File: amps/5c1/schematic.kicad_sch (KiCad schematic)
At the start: 21 parts, among them T1 SE 5k:8

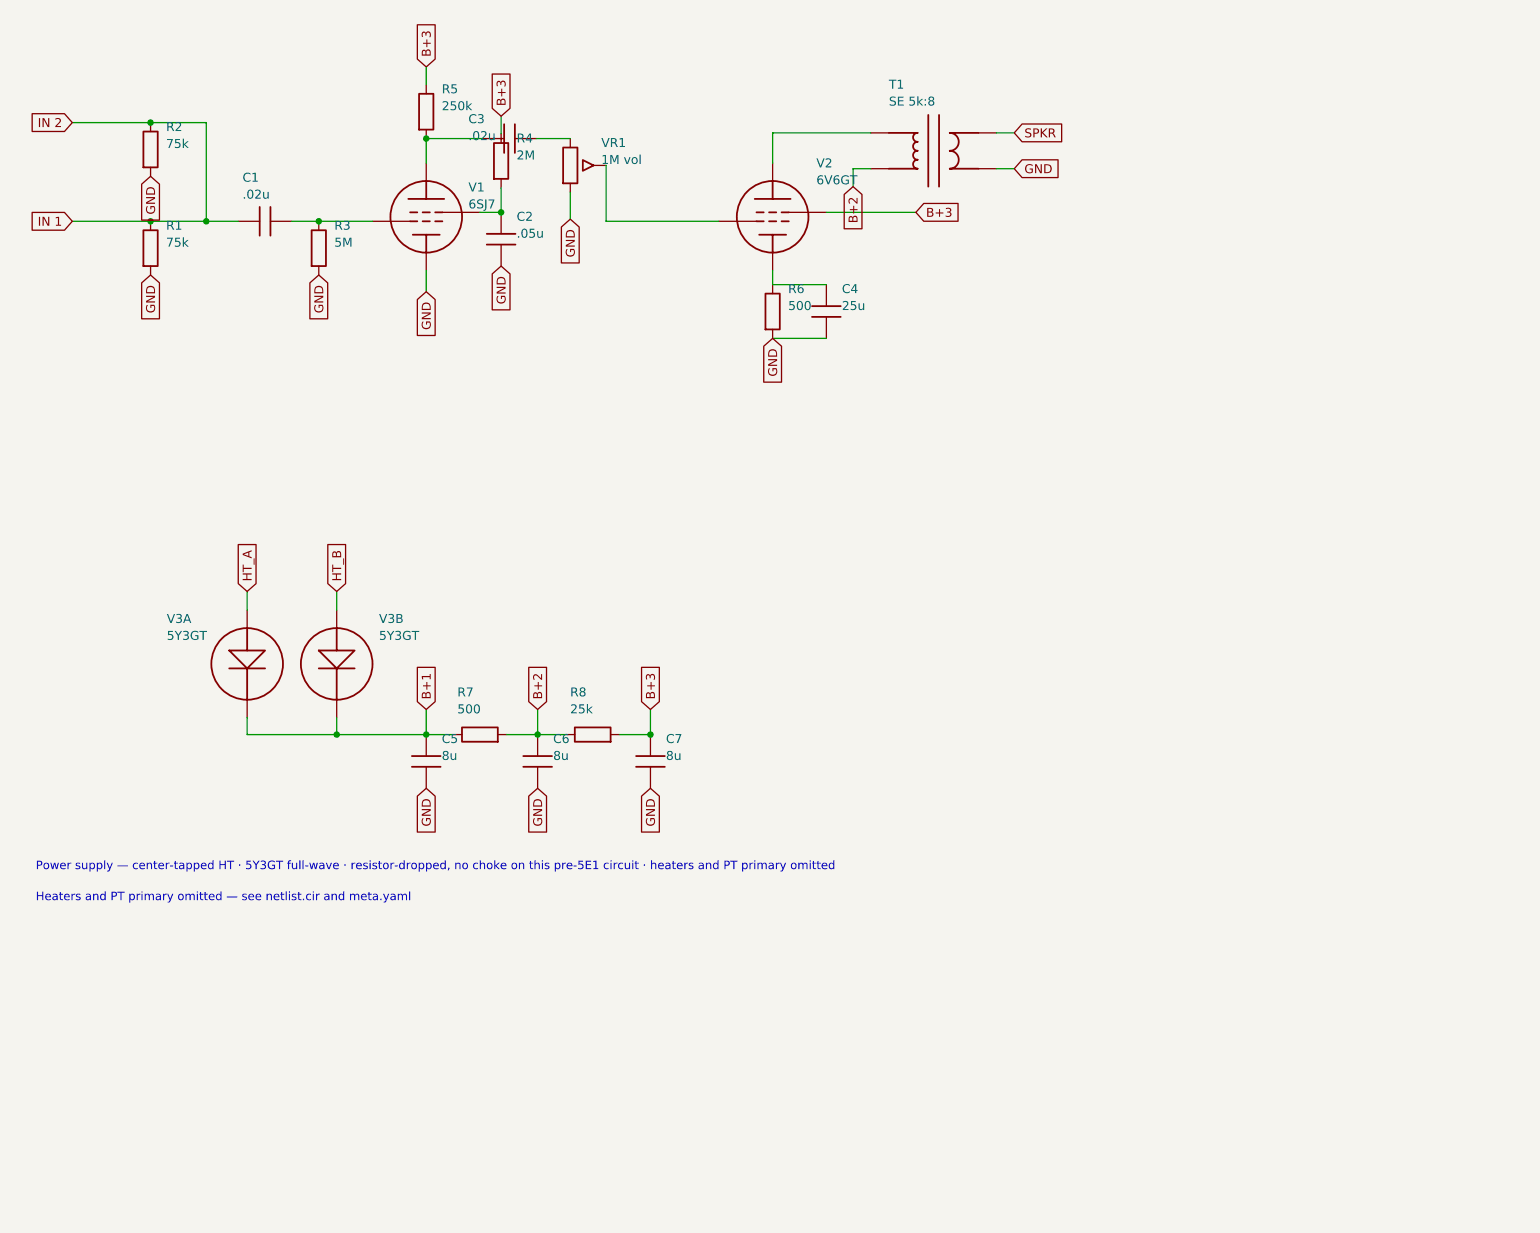
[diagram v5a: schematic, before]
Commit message: Add: real tube pin numbers and readable valve glyphs on every schematic
Phase B of the drawing program. A factory service sheet numbers every tube
pin, because the number is what a technician puts a probe on. This corpus
printed none, and the numbers hidden in its symbols were positional
placeholders (P=1, G=2, K=3) that would have published a 6V6GT's plate as
pin 1 when it is pin 3.

1055 electrodes now carry the real number, 1027 lettered (27 are shared
filaments deduped, 1 dropped for want of clear space on the 6G2). Resolved per
instance from reference/tubes/<slug>.yaml through the same alias resolution the
layout renderer uses, so a 12AX7 section and a 6SL7 section each get their own
basing. A valve whose basing the corpus does not carry prints nothing rather
than a wrong number.

Section letters and basing units are now separate things, which cost a detour
worth recording. The RCA 12AX7-A sheet reads "Pin 1 - Plate of Unit No.2 ...
Pin 6 - Plate of Unit No.1", so unit numbering is not pin order; the 5Y3 and
GZ34 number their units in opposite pin order, so nothing positional can
express it. But the section LETTER is a designator, not a basing fact: this
corpus, like every technician, calls the first stage in signal order V1A, and
five amps' prose already did. On four amps the factory sheets put that first
stage on the other half -- the AA764's own schematic prints +200 V on pin 1 --
so those drawings now state their unit explicitly, each citing its source, and
no letter, netlist, parts list or layout comment changed. 183 layout comments
agree with the printed numbers, 0 disagree. A guard fires if two halves of one
bottle resolve to the same unit, which is exactly how this was found.

Glyphs: the cathode gains a bracket and filament hairpin so it can no longer be
confused with the plate bar, the pentode's screen sits on its own row, and a
rectifier draws as one envelope over its sections instead of two apparent
bottles. Line weights are scaled per sheet to a co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
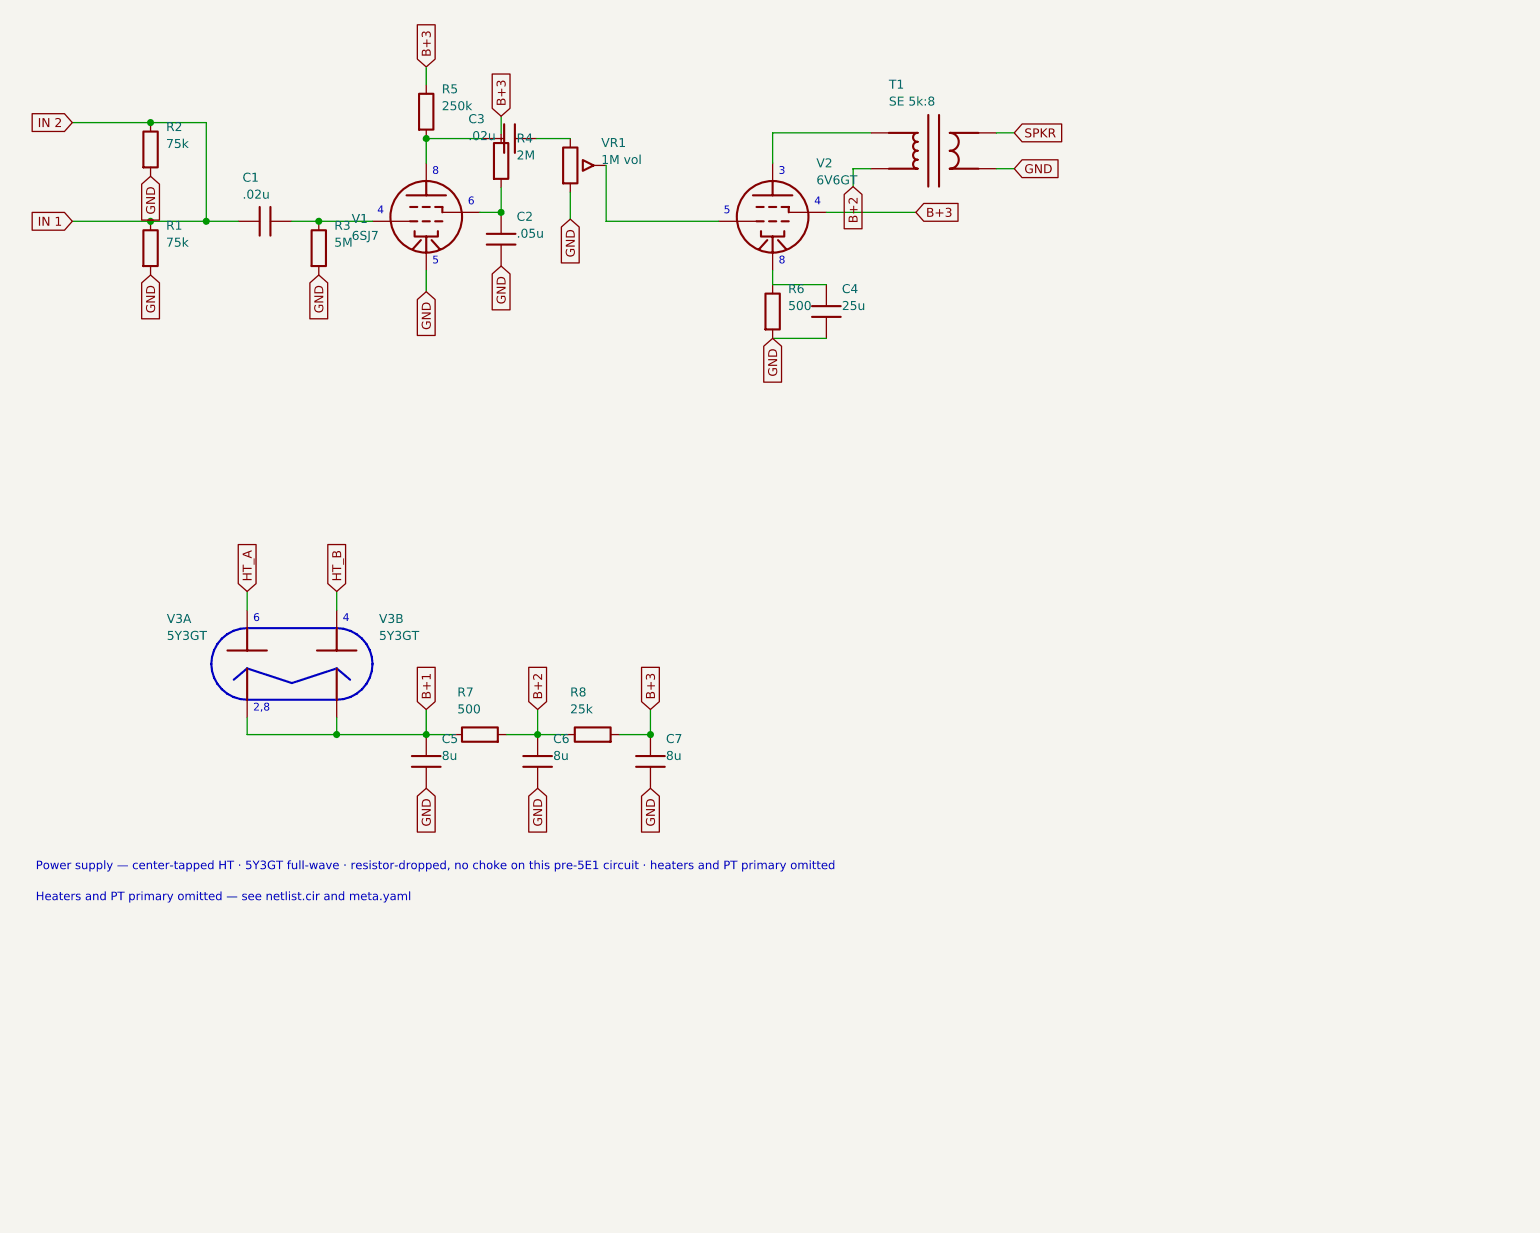
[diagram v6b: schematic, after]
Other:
- note added: "2,8"
- note added: "3"
- note added: "4"
- note added: "5"
- note added: "6"
- note added: "8"
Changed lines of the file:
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@@
   (wire (pts (xy 17.8816 38.913) (xy 28.9816 38.913))
     (stroke (width 0) (type default)))
-  (junction (at 28.9816 38.913) (diameter 0) (color 0 0 0 0))
+  (junction (at 28.9816 38.913) (diameter 1) (color 0 0 0 0))
   (symbol (lib_id "cx:R") (at 28.9816 42.723 0) (unit 1)
     (in_bom yes) (on_board yes)
@@
   (wire (pts (xy 17.8816 24.913) (xy 28.9816 24.913))
     (stroke (width 0) (type default)))
-  (junction (at 28.9816 24.913) (diameter 0) (color 0 0 0 0))
+  (junction (at 28.9816 24.913) (diameter 1) (color 0 0 0 0))
   (symbol (lib_id "cx:R") (at 28.9816 28.723 0) (unit 1)
     (in_bom yes) (on_board yes)
@@
   (wire (pts (xy 36.8816 24.913) (xy 36.8816 38.913))
     (stroke (width 0) (type default)))
-  (junction (at 36.8816 38.913) (diameter 0) (color 0 0 0 0))
+  (junction (at 36.8816 38.913) (diameter 1) (color 0 0 0 0))
   (symbol (lib_id "cx:C") (at 45.2216 38.913 90) (unit 1)
     (in_bom yes) (on_board yes)
@@
   (wire (pts (xy 49.0316 38.913) (xy 52.8416 38.913))
     (stroke (width 0) (type default)))
-  (junction (at 52.8416 38.913) (diameter 0) (color 0 0 0 0))
+  (junction (at 52.8416 38.913) (diameter 1) (color 0 0 0 0))
   (symbol (lib_id "cx:R") (at 52.8416 42.723 0) (unit 1)
     (in_bom yes) (on_board yes)
@@
   (symbol (lib_id "cx:PENTODE") (at 68.0816 38.278 0) (unit 1)
     (in_bom yes) (on_board yes)
-    (property "Reference" "V1" (at 74.0616 34.098 0) (effects (font (size 1.27 1.27)) (justify left)))
-    (property "Value" "6SJ7" (at 74.0616 36.498 0) (effects (font (size 1.27 1.27)) (justify left))))
+    (property "Reference" "V1" (at 57.5067 38.558 0) (effects (font (size 1.27 1.27)) (justify left)))
+    (property "Value" "6SJ7" (at 57.5067 40.958 0) (effects (font (size 1.27 1.27)) (justify left))))
   (wire (pts (xy 68.0816 45.898) (xy 68.0816 48.898))
     (stroke (width 0) (type default)))
@@
   (global_label "B+3" (shape input) (at 68.0816 17.018 90)
     (effects (font (size 1.27 1.27)) (justify left)))
-  (junction (at 68.0816 27.178) (diameter 0) (color 0 0 0 0))
+  (junction (at 68.0816 27.178) (diameter 1) (color 0 0 0 0))
   (wire (pts (xy 68.0816 27.178) (xy 76.0816 27.178))
     (stroke (width 0) (type default)))
@@
   (wire (pts (xy 75.7016 37.643) (xy 78.7016 37.643))
     (stroke (width 0) (type default)))
-  (junction (at 78.7016 37.643) (diameter 0) (color 0 0 0 0))
+  (junction (at 78.7016 37.643) (diameter 1) (color 0 0 0 0))
   (symbol (lib_id "cx:C") (at 78.7016 41.453 0) (unit 1)
     (in_bom yes) (on_board yes)
@@
   (wire (pts (xy 55.3816 111.713) (xy 68.0816 111.713))
     (stroke (width 0) (type default)))
-  (junction (at 55.3816 111.713) (diameter 0) (color 0 0 0 0))
-  (junction (at 68.0816 111.713) (diameter 0) (color 0 0 0 0))
+  (junction (at 55.3816 111.713) (diameter 1) (color 0 0 0 0))
+  (junction (at 68.0816 111.713) (diameter 1) (color 0 0 0 0))
   (symbol (lib_id "cx:C") (at 68.0816 115.523 0) (unit 1)
     (in_bom yes) (on_board yes)
@@
   (wire (pts (xy 79.5016 111.713) (xy 83.8816 111.713))
     (stroke (width 0) (type default)))
-  (junction (at 83.8816 111.713) (diameter 0) (color 0 0 0 0))
+  (junction (at 83.8816 111.713) (diameter 1) (color 0 0 0 0))
   (symbol (lib_id "cx:C") (at 83.8816 115.523 0) (unit 1)
     (in_bom yes) (on_board yes)
@@
   (wire (pts (xy 95.5016 111.713) (xy 99.8816 111.713))
     (stroke (width 0) (type default)))
-  (junction (at 99.8816 111.713) (diameter 0) (color 0 0 0 0))
+  (junction (at 99.8816 111.713) (diameter 1) (color 0 0 0 0))
   (symbol (lib_id "cx:C") (at 99.8816 115.523 0) (unit 1)
     (in_bom yes) (on_board yes)
@@
   (global_label "B+3" (shape input) (at 99.8816 108.153 90)
     (effects (font (size 1.27 1.27)) (justify left)))
+  (polyline (pts (xy 55.3816 96.613) (xy 56.3726 96.711) (xy 57.3256 97) (xy 58.2036 97.469) (xy 58.9736 98.101) (xy 59.6056 98.871) (xy 60.0746 99.749) (xy 60.3636 100.702) (xy 60.4616 101.693) (xy 60.3636 102.684) (xy 60.0746 103.637) (xy 59.6056 104.515) (xy 58.9736 105.285) (xy 58.2036 105.917) (xy 57.3256 106.386) (xy 56.3726 106.675) (xy 55.3816 106.773) (xy 42.6816 106.773) (xy 41.6906 106.675) (xy 40.7376 106.386) (xy 39.8596 105.917) (xy 39.0896 105.285) (xy 38.4576 104.515) (xy 37.9886 103.637) (xy 37.6996 102.684) (xy 37.6016 101.693) (xy 37.6996 100.702) (xy 37.9886 99.749) (xy 38.4576 98.871) (xy 39.0896 98.101) (xy 39.8596 97.469) (xy 40.7376 97) (xy 41.6906 96.711) (xy 42.6816 96.613) (xy 55.3816 96.613))
+    (stroke (width 0.3) (type default) (color 197 163 255 1)) (fill (type none)))
+  (polyline (pts (xy 40.7816 103.928) (xy 42.6816 102.328) (xy 49.0316 104.408) (xy 55.3816 102.328) (xy 57.2816 103.928))
+    (stroke (width 0.3) (type default) (color 197 163 255 1)) (fill (type none)))
+  (text "8" (at 68.9316 31.928 0)
+    (effects (font (size 1.1 1.1)) (justify left)))
+  (text "4" (at 61.1344 37.513 0)
+    (effects (font (size 1.1 1.1)) (justify left)))
+  (text "6" (at 73.9816 36.243 0)
+    (effects (font (size 1.1 1.1)) (justify left)))
+  (text "5" (at 68.9316 44.628 0)
+    (effects (font (size 1.1 1.1)) (justify left)))
+  (text "3" (at 118.062 31.928 0)
+    (effects (font (size 1.1 1.1)) (justify left)))
+  (text "5" (at 110.264 37.513 0)
+    (effects (font (size 1.1 1.1)) (justify left)))
+  (text "4" (at 123.112 36.243 0)
+    (effects (font (size 1.1 1.1)) (justify left)))
+  (text "8" (at 118.062 44.628 0)
+    (effects (font (size 1.1 1.1)) (justify left)))
+  (text "6" (at 43.5316 95.343 0)
+    (effects (font (size 1.1 1.1)) (justify left)))
+  (text "2,8" (at 43.5316 108.043 0)
+    (effects (font (size 1.1 1.1)) (justify left)))
+  (text "4" (at 56.2316 95.343 0)
+    (effects (font (size 1.1 1.1)) (justify left)))
   (text "Power supply — center-tapped HT · 5Y3GT full-wave · resistor-dropped, no choke on this pre-5E1 circuit · heaters and PT primary omitted" (at 12.7 130.491 0)
     (effects (font (size 1.2 1.2)) (justify left)))

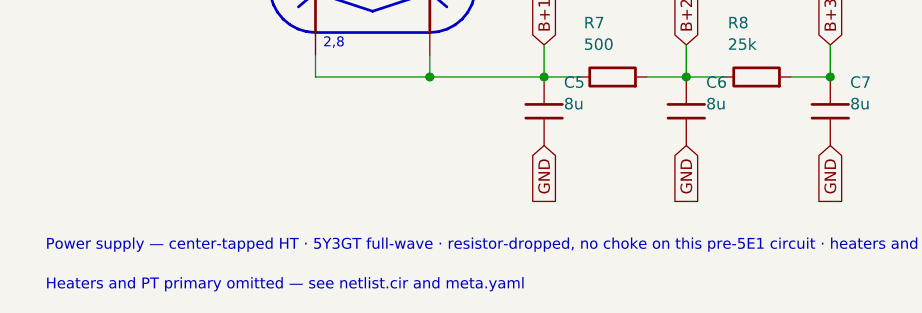
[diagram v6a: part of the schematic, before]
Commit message: Fix: schematic sheet notes no longer name repository files
Thirty-seven committed sheets rendered footnotes and section notes such as
"Heaters and PT primary omitted — see netlist.cir and meta.yaml" or
"excluded from netlist.cir (notes.md)" to visitors through KiCanvas. The
prose sweeps never counted sheets. Rewritten in the site's own words — the
netlist, the sources list, the circuit story, the parts list, the board
drawing — in 59 strings across 33 draw scripts, keeping every technical
claim as it was; the three tone sheets (6G4, 6G5, 6G6-B) are under repair
elsewhere and keep theirs for now. The sweep touched only strings passed to
the sheet's note, text, caption and footnote calls, never a path or a value.

Gates: check_schematics 40/0, connectivity 0 isolated pins;
verify_schematic_nets 40 clean; only the regenerated sheets and their served
copies changed.

Co-Authored-By: Claude Fable 5.1 <noreply@anthropic.com>
Claude-Session: https://claude.ai/code/session_01KBMfdh37HmCL2iWcBiL5J1
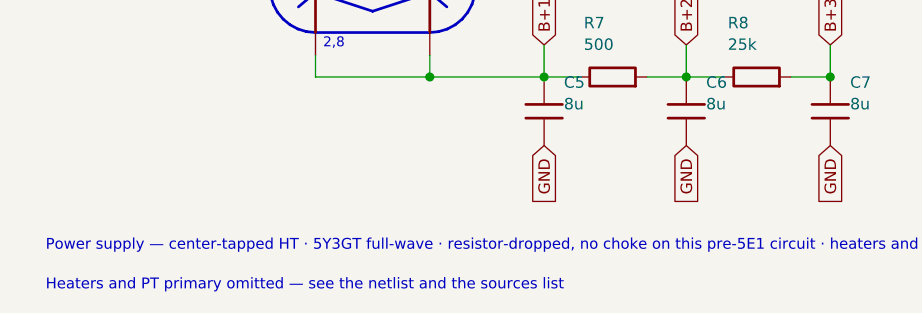
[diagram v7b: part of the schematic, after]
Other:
- note added: "Heaters and PT primary omitted — see the netlist and the sources list"
- note removed: "Heaters and PT primary omitted — see netlist.cir and meta.yaml"
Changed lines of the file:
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@@
   (text "Power supply — center-tapped HT · 5Y3GT full-wave · resistor-dropped, no choke on this pre-5E1 circuit · heaters and PT primary omitted" (at 12.7 130.491 0)
     (effects (font (size 1.2 1.2)) (justify left)))
-  (text "Heaters and PT primary omitted — see netlist.cir and meta.yaml" (at 12.7 134.891 0)
+  (text "Heaters and PT primary omitted — see the netlist and the sources list" (at 12.7 134.891 0)
     (effects (font (size 1.2 1.2)) (justify left)))
   (sheet_instances (path "/" (page "1")))
